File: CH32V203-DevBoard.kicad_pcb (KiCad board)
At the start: 2 copper layers, 20.3 x 50.8 mm, 41 parts, among them J1 USB_C_Receptacle_USB2.0_16P, J2 USB_C_Receptacle_USB2.0_16P, Q1 AO3401A, Q2 AO3401A, SW1 SW_Push, SW2 SW_Push, U1 CH32V203C8T6, U2 RT9080-33GJ5

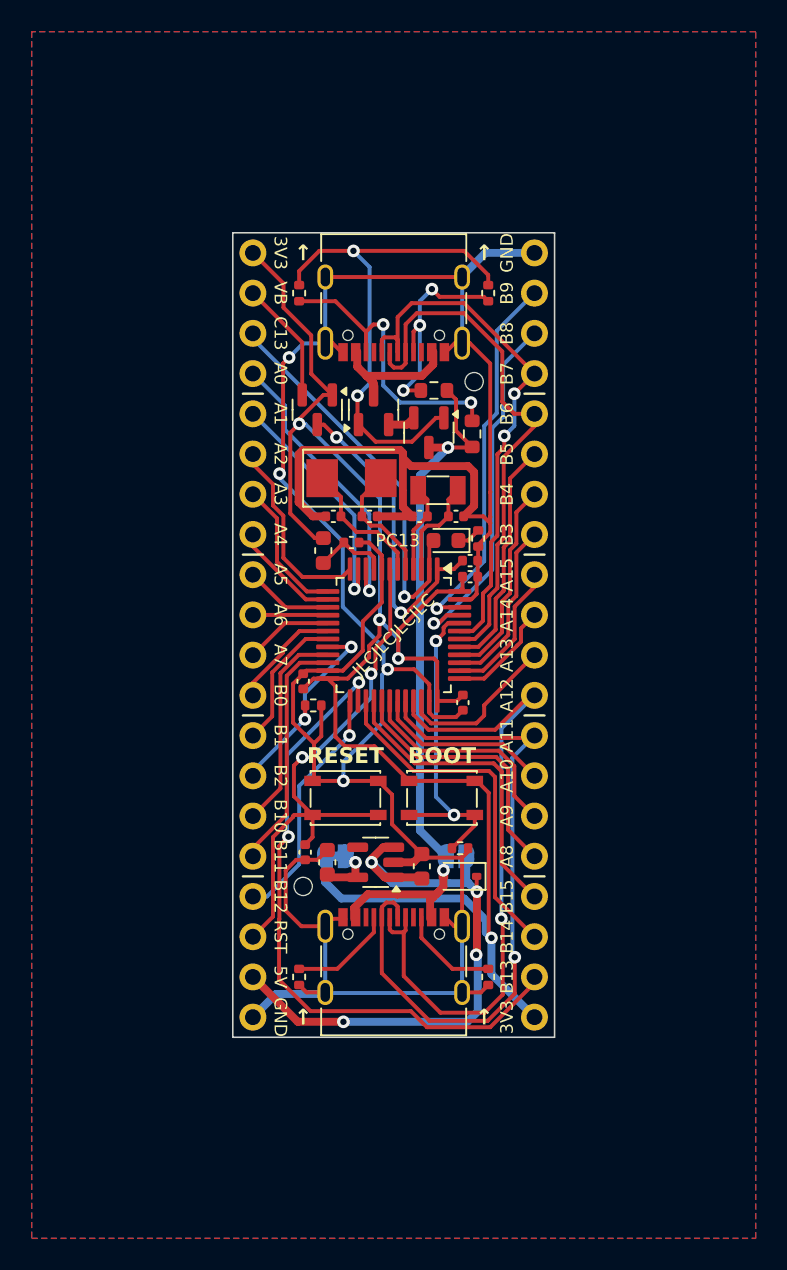
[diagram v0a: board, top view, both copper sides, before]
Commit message: 配線・シルクを微調整
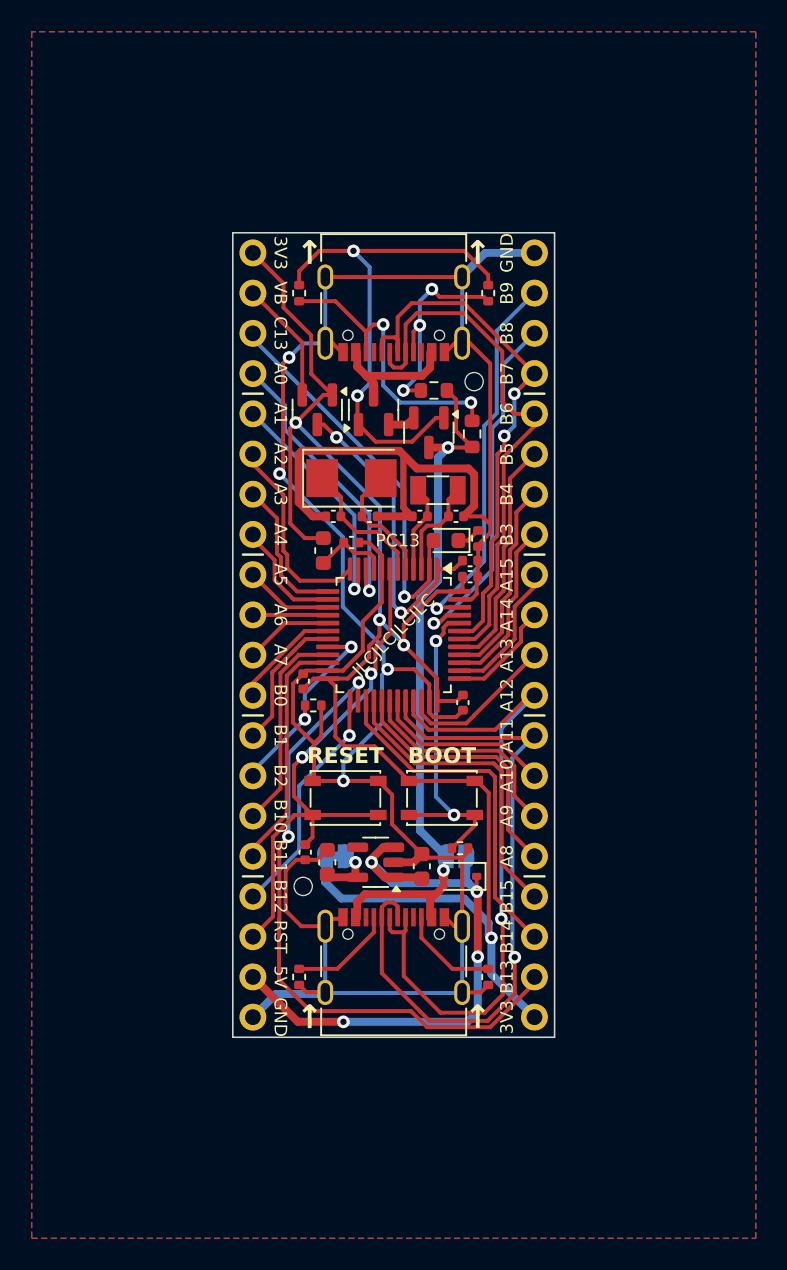
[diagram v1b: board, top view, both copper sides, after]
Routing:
- net +3V3: track 106.8 -> 104.7 mm
- net +5V: track 39.0 -> 39.6 mm
- net PB12: track 15.4 -> 14.9 mm

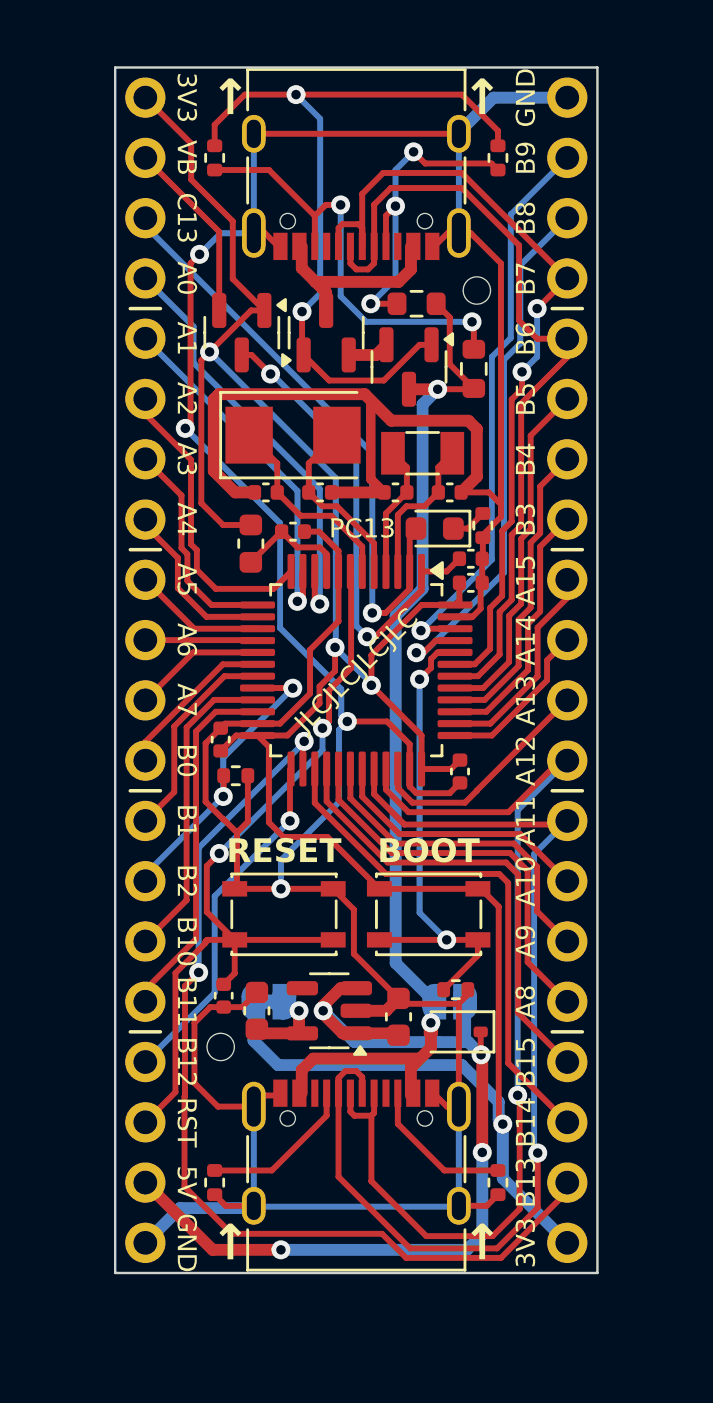
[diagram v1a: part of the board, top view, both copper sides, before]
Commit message: USB周りの配線や裏面シルクの修正
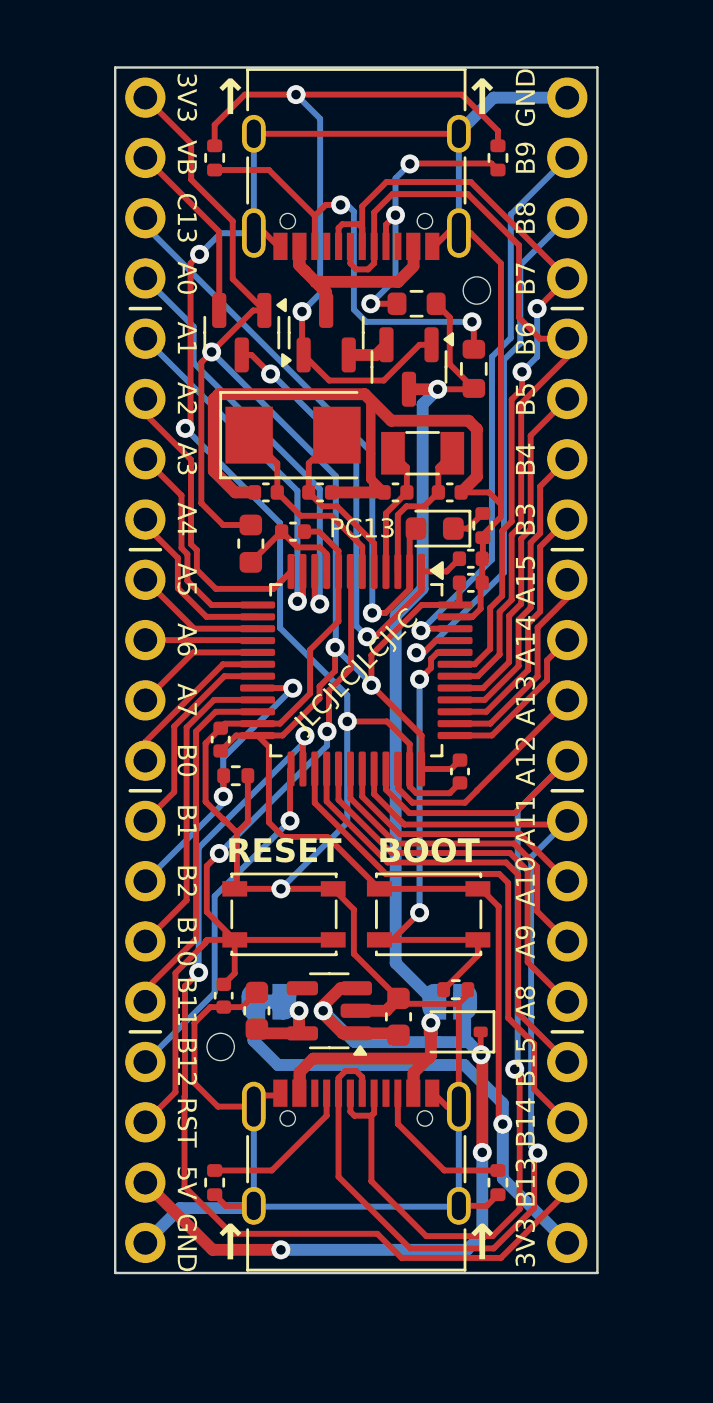
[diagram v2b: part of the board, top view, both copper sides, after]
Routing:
- net Net-(Q2-D): track 8.34 -> 7.08 mm
- net Net-(J2-CC1): track 14.0 -> 13.0 mm
- net PB7: track 34.4 -> 33.8 mm
- net VBUS: track 44.9 -> 44.3 mm
- net BOOT0: track 20.5 -> 21.0 mm

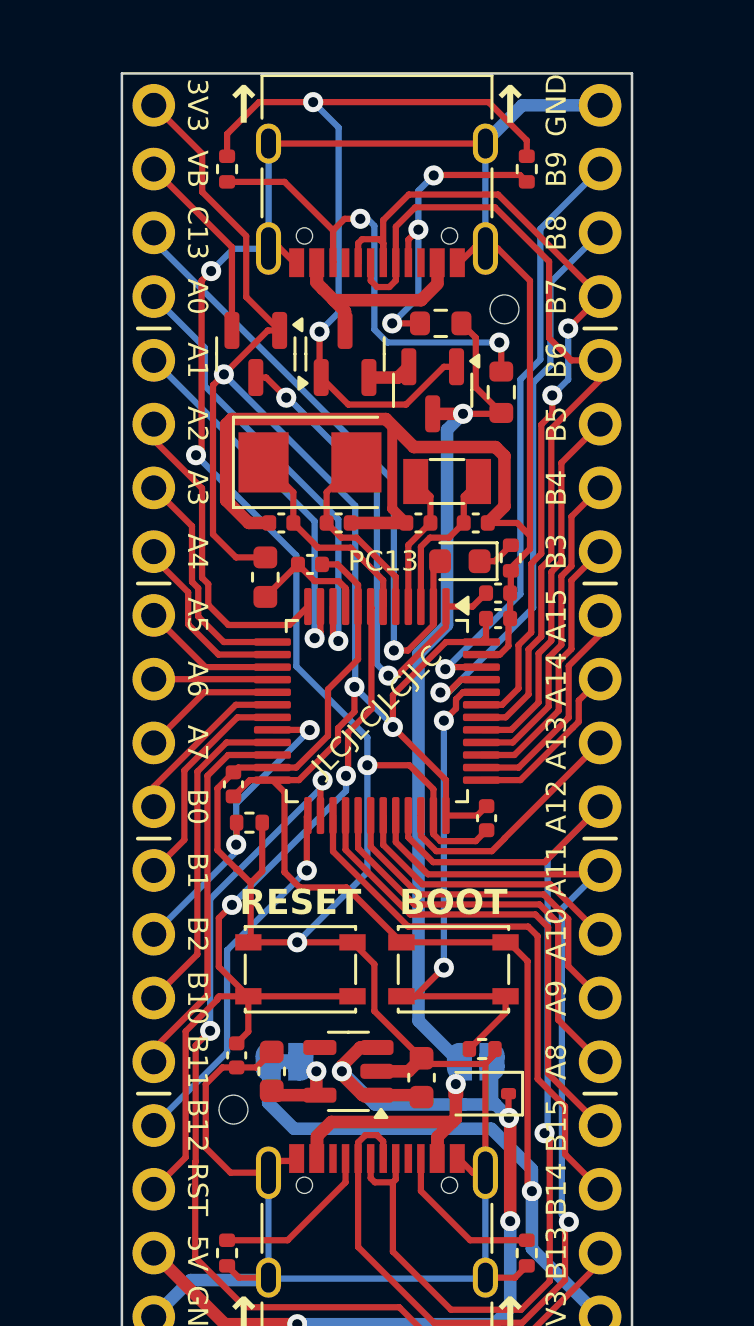
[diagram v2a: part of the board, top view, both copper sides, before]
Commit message: add usb2 device solder jumper
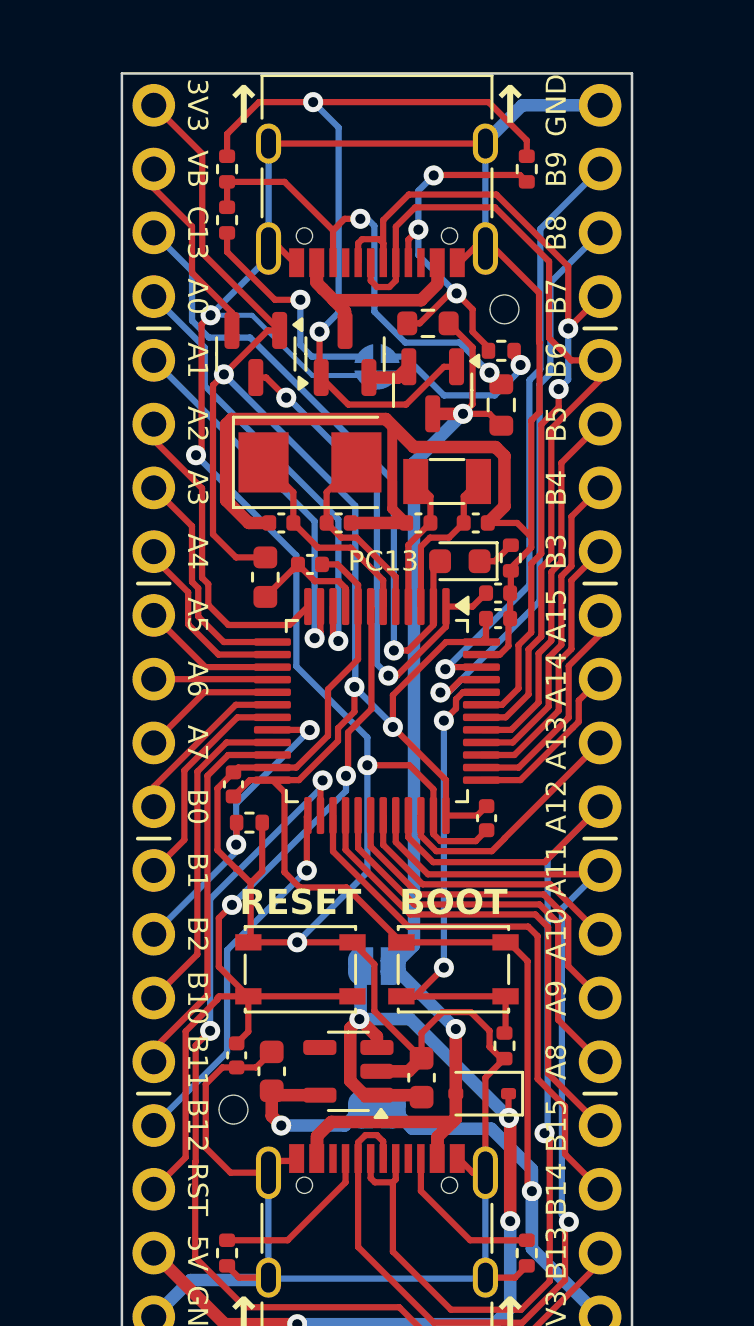
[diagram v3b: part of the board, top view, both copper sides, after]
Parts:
- added JP3: SolderJumper_2-to-1_Open, SolderJumper:SolderJumper-2-to-1_P0.9mm_Open, B.Cu at (137.2, 87.9)
- added R10: 5.1kΩ, Resistor_SMD:R_0402_1005Metric, F.Cu at (142.1, 87.2)
- added R11: 5.1kΩ, Resistor_SMD:R_0402_1005Metric, F.Cu at (131.2, 82.0)
- moved JP2 5.48 mm to (137.2, 111.8), turned to 180 degrees
- moved JP1 4.15 mm to (137.2, 117.5), turned to 0 degrees
- moved R2 0.90 mm to (142.2, 114.9), turned to 90 degrees
- moved R7 0.51 mm to (142.1, 89.4)
- moved R6 0.51 mm to (139.2, 86.2)
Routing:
- net GND: track 193.8 -> 203.0 mm
- net Net-(JP3-B): track 0.00 -> 9.11 mm, vias 0 -> 1
- net Net-(JP3-A): track 0.00 -> 7.25 mm, vias 0 -> 1
- net +3V3: track 104.6 -> 97.9 mm
- net Net-(J2-CC1): track 13.0 -> 16.2 mm
- net Net-(JP1-A): track 3.78 -> 6.95 mm
- net +5V: track 39.6 -> 41.7 mm
- net BOOT0: track 21.0 -> 19.8 mm
- net PC13: track 25.2 -> 26.2 mm
- net VBUS: track 44.3 -> 45.1 mm
- net PB7: track 33.8 -> 34.5 mm
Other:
- board text removed: "JLCJLCJLCJLC"

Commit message: pulldown resistor fix
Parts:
- R10, R11: value 5.1kΩ -> 4.7kΩ
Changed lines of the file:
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@@
 			)
 		)
-		(property "Value" "5.1kΩ"
+		(property "Value" "4.7kΩ"
 			(at 0 1.17 180)
 			(layer "F.Fab")
@@
 			)
 		)
-		(property "LCSC" "C25905"
+		(property "LCSC" "C25900"
 			(at 0 0 180)
 			(unlocked yes)
@@
 			)
 		)
-		(property "Value" "5.1kΩ"
+		(property "Value" "4.7kΩ"
 			(at 0 1.17 -90)
 			(layer "F.Fab")
@@
 			)
 		)
-		(property "LCSC" "C25905"
+		(property "LCSC" "C25900"
 			(at 0 0 90)
 			(unlocked yes)
@@
 			)
 		)
+		(property "JLCPCB Rotation Offset" "0"
+			(at 0 0 180)
+			(unlocked yes)
+			(layer "F.Fab")
+			(hide yes)
+			(effects
+				(font
+					(size 1 1)
+					(thickness 0.15)
+				)
+			)
+		)
 		(property ki_fp_filters "Crystal*")
 		(sheetname "ルート")
@@
 			)
 		)
+		(property "JLCPCB Rotation Offset" "0"
+			(at 0 0 0)
+			(unlocked yes)
+			(layer "F.Fab")
+			(hide yes)
+			(effects
+				(font
+					(size 1 1)
+					(thickness 0.15)
+				)
+			)
+		)
 		(property ki_fp_filters "Crystal*")
 		(sheetname "ルート")
@@
 	)
 	(zone
-		(net 5)
-		(net_name "PC14")
-		(layer "F.Cu")
-		(name "$teardrop_padvia$")
-		(hatch full 0.1)
-		(priority 30000)
-		(attr
-			(teardrop
-				(type padvia)
-			)
-		)
-		(connect_pads yes
-			(clearance 0)
-		)
-		(min_thickness 0.0254)
-		(filled_areas_thickness no)
-		(fill yes
-			(thermal_gap 0.5)
-			(thermal_bridge_width 0.5)
-			(island_removal_mode 1)
-			(island_area_min 10)
-		)
-		(polygon
-			(pts
-				(xy 140.492 93.419964) (xy 140.742 93.419964) (xy 141.241155 93.356) (xy 141.204 92.455) (xy 140.704 92.314867)
-			)
-		)
-	)
-	(zone
 		(net 21)
 		(net_name "PB0")
@@
 	)
 	(zone
+		(net 8)
+		(net_name "PD1")
+		(layer "F.Cu")
+		(name "$teardrop_padvia$")
+		(hatch full 0.1)
+		(priority 30001)
+		(attr
+			(teardrop
+				(type padvia)
+			)
+		)
+		(connect_pads yes
+			(clearance 0)
+		)
+		(min_thickness 0.0254)
+		(filled_areas_thickness no)
+		(fill yes
+			(thermal_gap 0.5)
+			(thermal_bridge_width 0.5)
+			(island_removal_mode 1)
+			(island_area_min 10)
+		)
+		(polygon
+			(pts
+				(xy 133.705 93.616543) (xy 133.955 93.616543) (xy 133.643 91.40929) (xy 132.643 91.693) (xy 132.209051 92.894)
+			)
+		)
+	)
+	(zone
 		(net 29)
 		(net_name "PA8")
@@
 	)
 	(zone
-		(net 26)
-		(net_name "PB13")
+		(net 5)
+		(net_name "PC14")
 		(layer "F.Cu")
 		(name "$teardrop_padvia$")
 		(hatch full 0.1)
-		(priority 30029)
+		(priority 30002)
 		(attr
 			(teardrop
@@
 		(polygon
 			(pts
-				(xy 144.987923 124.4563) (xy 145.1647 124.633077) (xy 146.375281 123.975298) (xy 146.050707 123.189293)
-				(xy 145.2 123.19)
+				(xy 140.492 93.419964) (xy 140.742 93.419964) (xy 141.241155 93.356) (xy 141.204 92.455) (xy 140.704 92.314867)
 			)
 		)
 	)
 	(zone
-		(net 34)
-		(net_name "PA15")
+		(net 26)
+		(net_name "PB13")
 		(layer "F.Cu")
 		(name "$teardrop_padvia$")
 		(hatch full 0.1)
-		(priority 30026)
+		(priority 30029)
 		(attr
 			(teardrop
@@
 		(polygon
 			(pts
-				(xy 145.287171 99.138052) (xy 145.463948 99.314829) (xy 146.651041 98.391041) (xy 146.050707 97.789293)
-				(xy 145.2 97.79)
+				(xy 144.987923 124.4563) (xy 145.1647 124.633077) (xy 146.375281 123.975298) (xy 146.050707 123.189293)
+				(xy 145.2 123.19)
 			)
 		)
 	)
 	(zone
-		(net 6)
-		(net_name "PC15")
+		(net 34)
+		(net_name "PA15")
 		(layer "F.Cu")
 		(name "$teardrop_padvia$")
 		(hatch full 0.1)
-		(priority 30001)
+		(priority 30026)
 		(attr
 			(teardrop
@@
 		(polygon
 			(pts
-				(xy 139.166 93.419964) (xy 139.416 93.419964) (xy 139.204 92.314867) (xy 138.704 92.455) (xy 138.666845 93.356)
+				(xy 145.287171 99.138052) (xy 145.463948 99.314829) (xy 146.651041 98.391041) (xy 146.050707 97.789293)
+				(xy 145.2 97.79)
 			)
 		)
@@
 	)
 	(zone
+		(net 7)
+		(net_name "PD0")
+		(layer "F.Cu")
+		(name "$teardrop_padvia$")
+		(hatch full 0.1)
+		(priority 30000)
+		(attr
+			(teardrop
+				(type padvia)
+			)
+		)
+		(connect_pads yes
+			(clearance 0)
+		)
+		(min_thickness 0.0254)
+		(filled_areas_thickness no)
+		(fill yes
+			(thermal_gap 0.5)
+			(thermal_bridge_width 0.5)
+			(island_removal_mode 1)
+			(island_area_min 10)
+		)
+		(polygon
+			(pts
+				(xy 135.031 93.616543) (xy 135.281 93.616543) (xy 136.776949 92.894) (xy 136.343 91.693) (xy 135.343 91.40929)
+			)
+		)
+	)
+	(zone
 		(net 12)
 		(net_name "NRST")
@@
 	)
 	(zone
-		(net 8)
-		(net_name "PD1")
-		(layer "F.Cu")
-		(name "$teardrop_padvia$")
-		(hatch full 0.1)
-		(priority 30001)
-		(attr
-			(teardrop
-				(type padvia)
-			)
-		)
-		(connect_pads yes
-			(clearance 0)
-		)
-		(min_thickness 0.0254)
-		(filled_areas_thickness no)
-		(fill yes
-			(thermal_gap 0.5)
-			(thermal_bridge_width 0.5)
-			(island_removal_mode 1)
-			(island_area_min 10)
-		)
-		(polygon
-			(pts
-				(xy 133.705 93.616543) (xy 133.955 93.616543) (xy 133.643 91.40929) (xy 132.643 91.693) (xy 132.209051 92.894)
-			)
-		)
-	)
-	(zone
 		(net 3)
 		(net_name "GND")
@@
 	)
 	(zone
-		(net 7)
-		(net_name "PD0")
-		(layer "F.Cu")
-		(name "$teardrop_padvia$")
-		(hatch full 0.1)
-		(priority 30000)
-		(attr
-			(teardrop
-				(type padvia)
-			)
-		)
-		(connect_pads yes
-			(clearance 0)
-		)
-		(min_thickness 0.0254)
-		(filled_areas_thickness no)
-		(fill yes
-			(thermal_gap 0.5)
-			(thermal_bridge_width 0.5)
-			(island_removal_mode 1)
-			(island_area_min 10)
-		)
-		(polygon
-			(pts
-				(xy 135.031 93.616543) (xy 135.281 93.616543) (xy 136.776949 92.894) (xy 136.343 91.693) (xy 135.343 91.40929)
-			)
-		)
-	)
-	(zone
 		(net 3)
 		(net_name "GND")
@@
 			)
 		)
+	)
+	(zone
+		(net 6)
+		(net_name "PC15")
+		(layer "F.Cu")
+		(name "$teardrop_padvia$")
+		(hatch full 0.1)
+		(priority 30003)
+		(attr
+			(teardrop
+				(type padvia)
+			)
+		)
+		(connect_pads yes
+			(clearance 0)
+		)
+		(min_thickness 0.0254)
+		(filled_areas_thickness no)
+		(fill yes
+			(thermal_gap 0.5)
+			(thermal_bridge_width 0.5)
+			(island_removal_mode 1)
+			(island_area_min 10)
+		)
+		(polygon
+			(pts
+				(xy 139.166 93.419964) (xy 139.416 93.419964) (xy 139.204 92.314867) (xy 138.704 92.455) (xy 138.666845 93.356)
+			)
+		)
